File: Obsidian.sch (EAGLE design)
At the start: 33 parts, among them Q1 BS250, Q2 BS250, Q3 BS250

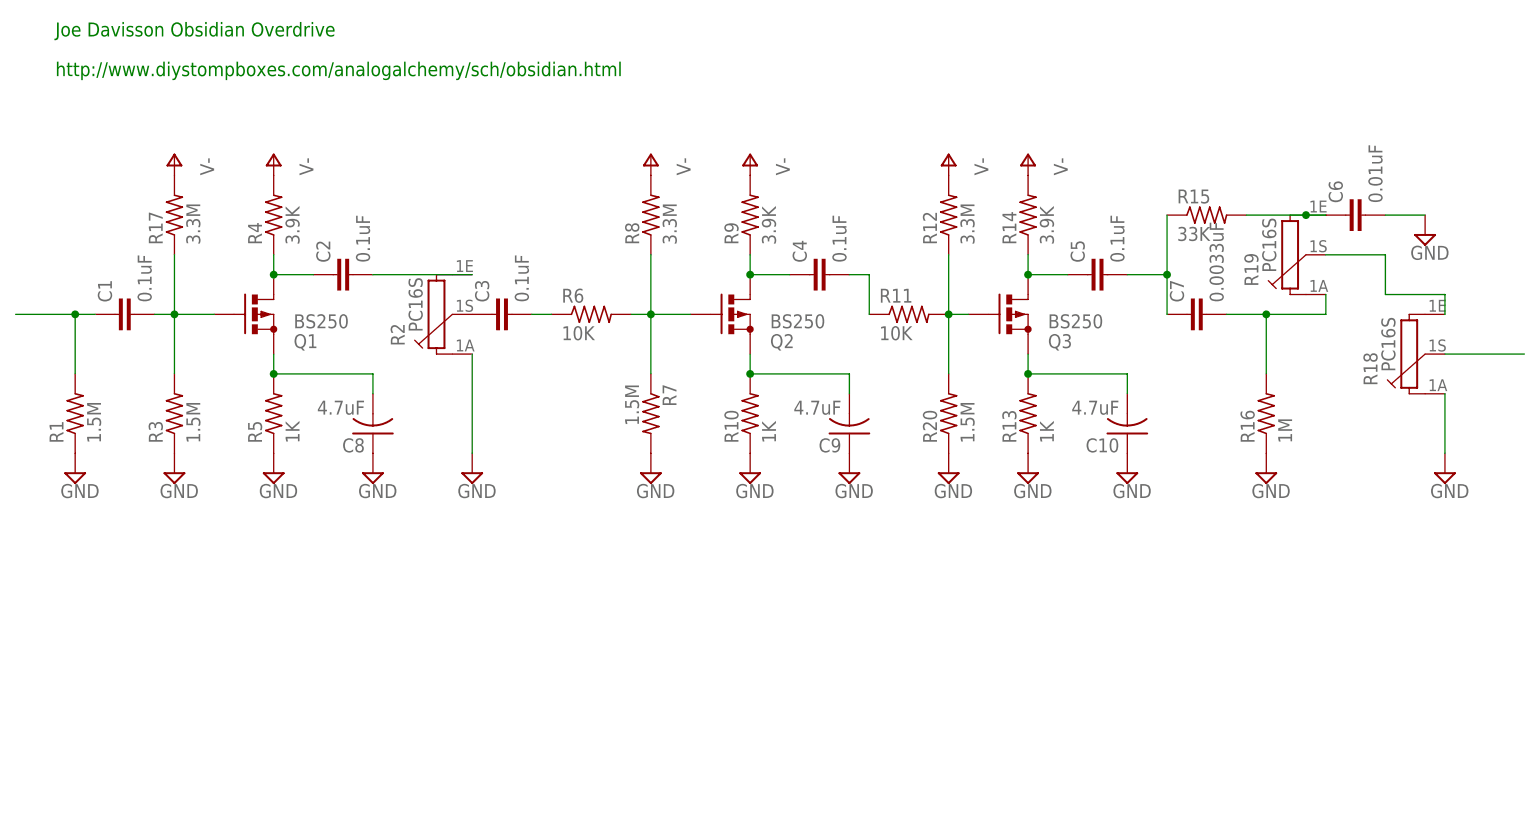
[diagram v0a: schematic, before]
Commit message: Found parts libs for pots, jacks, etc!
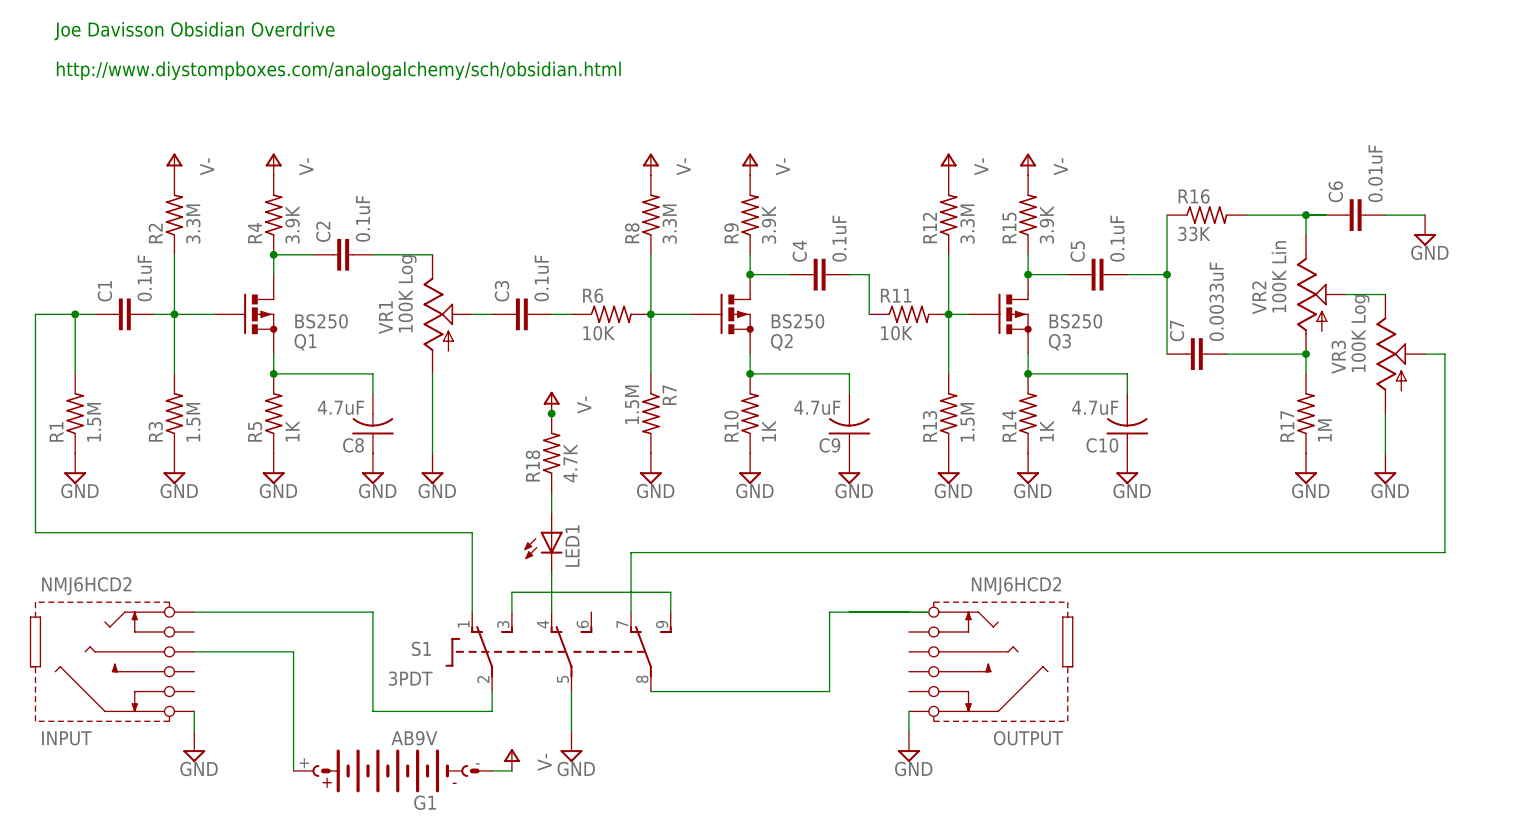
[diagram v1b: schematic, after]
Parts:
- removed R19: PC16S, piher:PC16S
- removed R20: 1.5M, resistor:R-US_0207/7
- added G1: AB9V, battery:AB9V
- added INPUT, OUTPUT: NMJ6HCD2, audio:NMJ6HCD2
- added LED1: (no value), led:LED5MM
- added S1: 3PDT, switch:3PDT
- added VR1, VR3: 100K Log, MusicThingModular:9MM_SNAP-IN_POT_
- added VR2: 100K Lin, MusicThingModular:9MM_SNAP-IN_POT_
- R13: value 1K -> 1.5M; device rcl:R-US_0204/7 -> resistor:R-US_0207/7
- R14: value 3.9K -> 1K
- R15: value 33K -> 3.9K
- R16: value 1M -> 33K
- R17: value 3.3M -> 1M
- R18: value PC16S -> 4.7K; device piher:PC16S -> rcl:R-US_0204/7
- R2: value PC16S -> 3.3M; device piher:PC16S -> rcl:R-US_0204/7
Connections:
- new net N$20: G1.+, INPUT.RING
- new net N$21: LED1.C, S1.O2
- new net N$22: INPUT.TIP, S1.P1
- new net N$23: OUTPUT.TIP
- new net N$24: S1.S1, S1.S3
- new net N$25: S1.P3
- new net N$27: LED1.A, R18.1
- net GND: now also INPUT.SLEEVE, OUTPUT.SLEEVE, R14.1, R17.1, S1.P2, VR1.A; no longer R13.1, R16.1, R18.1A, R2.1A
- net N$10: now also R14.2; no longer R13.2
- net N$11: now also R13.2; no longer R20.2
- net N$13: now also C2.2, VR1.E; no longer C3.1, R2.1S
- net N$14: now also R16.2, VR2.E; no longer R15.2, R19.1E
- net N$15: now also C3.1, VR1.S; no longer C2.2, R2.1E
- net N$16: now also R16.1; no longer R15.1
- net N$17: now also R17.2, VR2.A; no longer R16.2, R19.1A
- net N$18: now also VR2.S, VR3.E; no longer R18.1E, R19.1S
- net N$19: now also S1.O3, VR3.S; no longer R18.1S
- net N$3: now also R2.1; no longer R17.1
- net N$5: now also S1.O1
- net N$8: now also R15.1; no longer R14.1
- net V-: now also G1.-, R15.2, R2.2; no longer R14.2, R17.2
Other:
- moved on the sheet: C2, C3, C7, R13, R14, R15, R16, R17, R6
